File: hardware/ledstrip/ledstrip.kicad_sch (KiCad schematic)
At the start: 11 parts, among them J1 Conn_ARM_JTAG_SWD_10, J2 USB_C_Receptacle_USB2.0_16P, U1 STM32G030K6Tx, U2 CP2102N-A02-GQFN20, U3 STUSB4500QTR, U4 USBLC6-2SC6

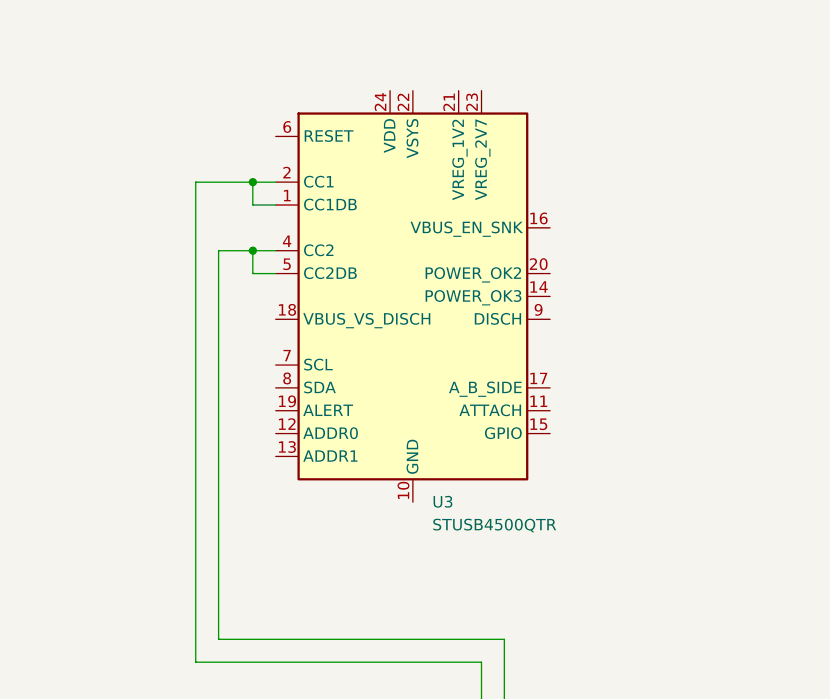
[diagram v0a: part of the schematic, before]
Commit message: Minor improvements, add I2C header for STUSB4500
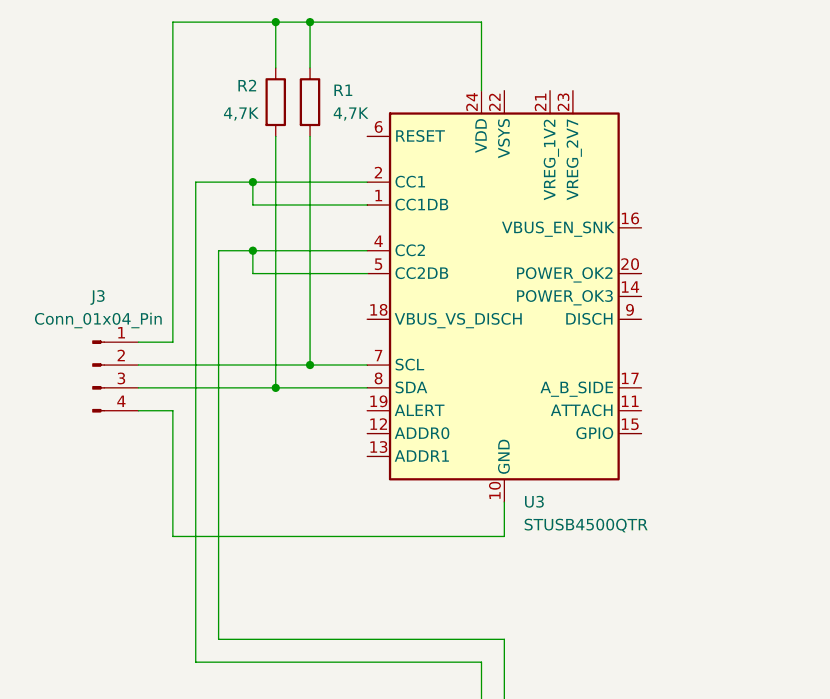
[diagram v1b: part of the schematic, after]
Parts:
- added J3: Conn_01x04_Pin, Connector_PinHeader_2.54mm:PinHeader_1x04_P2.54mm_Vertical, symbol Connector:Conn_01x04_Pin
- added R1, R2: 4,7K, symbol Device:R
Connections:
- net at U3.10 (GND), U3.25 (GND): now also J3.4 (Pin_4)
- net at U3.24 (VDD): now also J3.1 (Pin_1), R1.1, R2.1
- net at U3.7 (SCL): now also J3.2 (Pin_2), R1.2
- net at U3.8 (SDA): now also J3.3 (Pin_3), R2.2
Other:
- moved on the sheet: U3

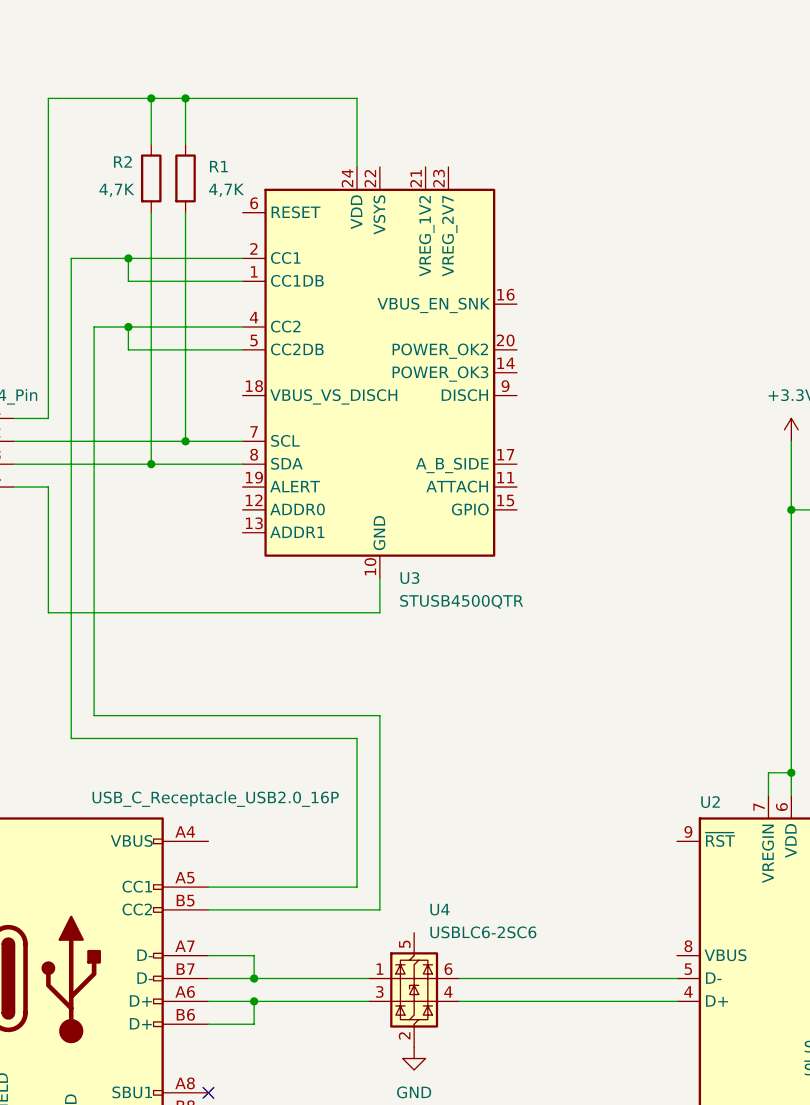
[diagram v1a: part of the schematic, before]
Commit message: Add TVS on CC lines, select a footprint for resistors.
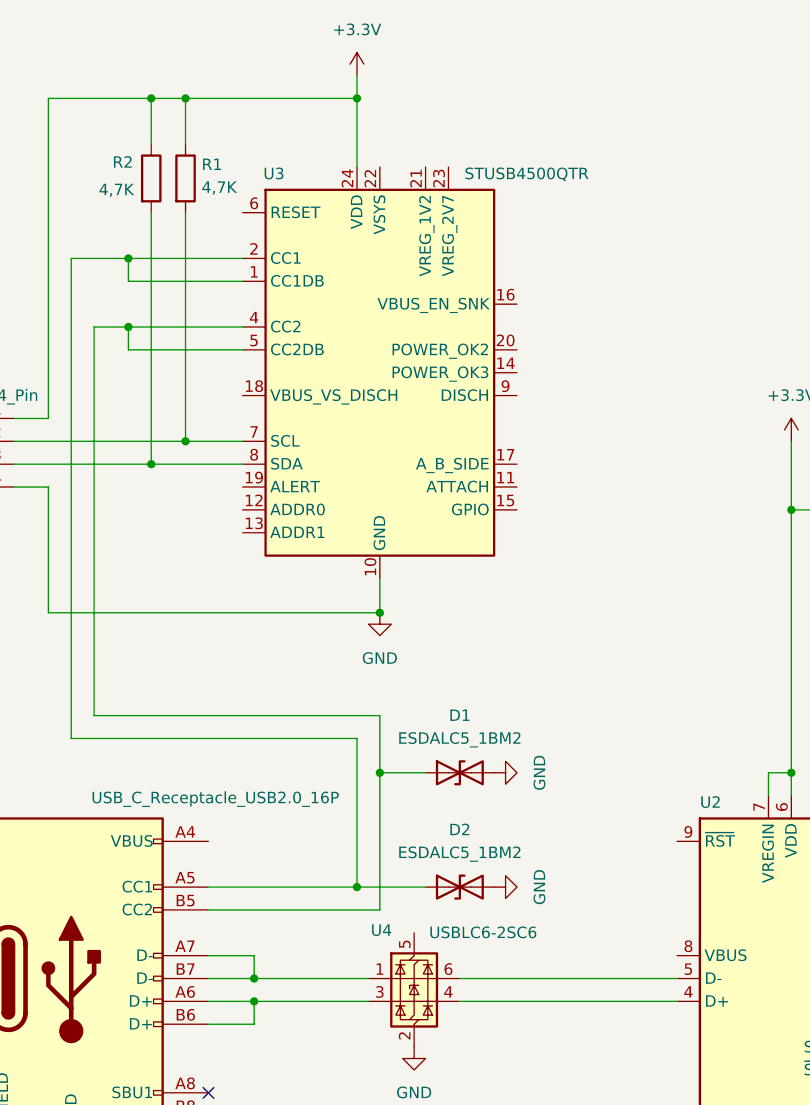
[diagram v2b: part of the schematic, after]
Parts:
- added D1, D2: ESDALC5_1BM2, Diode_SMD:D_SOD-882, symbol Device:D_TVS
- R1, R2: footprint (none) -> Resistor_SMD:R_0805_2012Metric; Distributor Link 1 (none) -> https://www.mouser.fr/ProductDetail/Panasonic/ERA-6ARW472V?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; Distributor Link 2 (none) -> https://www.digikey.com/en/products/detail/panasonic-electr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
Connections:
- net +3.3V: now also J3.1 (Pin_1), R1.1, R2.1, U3.24 (VDD)
- net GND: now also J3.4 (Pin_4), U3.10 (GND), U3.25 (GND), D1.2 (A2), D2.2 (A2)
- net at J2.A5 (CC1), U3.1 (CC1DB), U3.2 (CC1): now also D2.1 (A1)
- net at J2.B5 (CC2), U3.4 (CC2), U3.5 (CC2DB): now also D1.1 (A1)

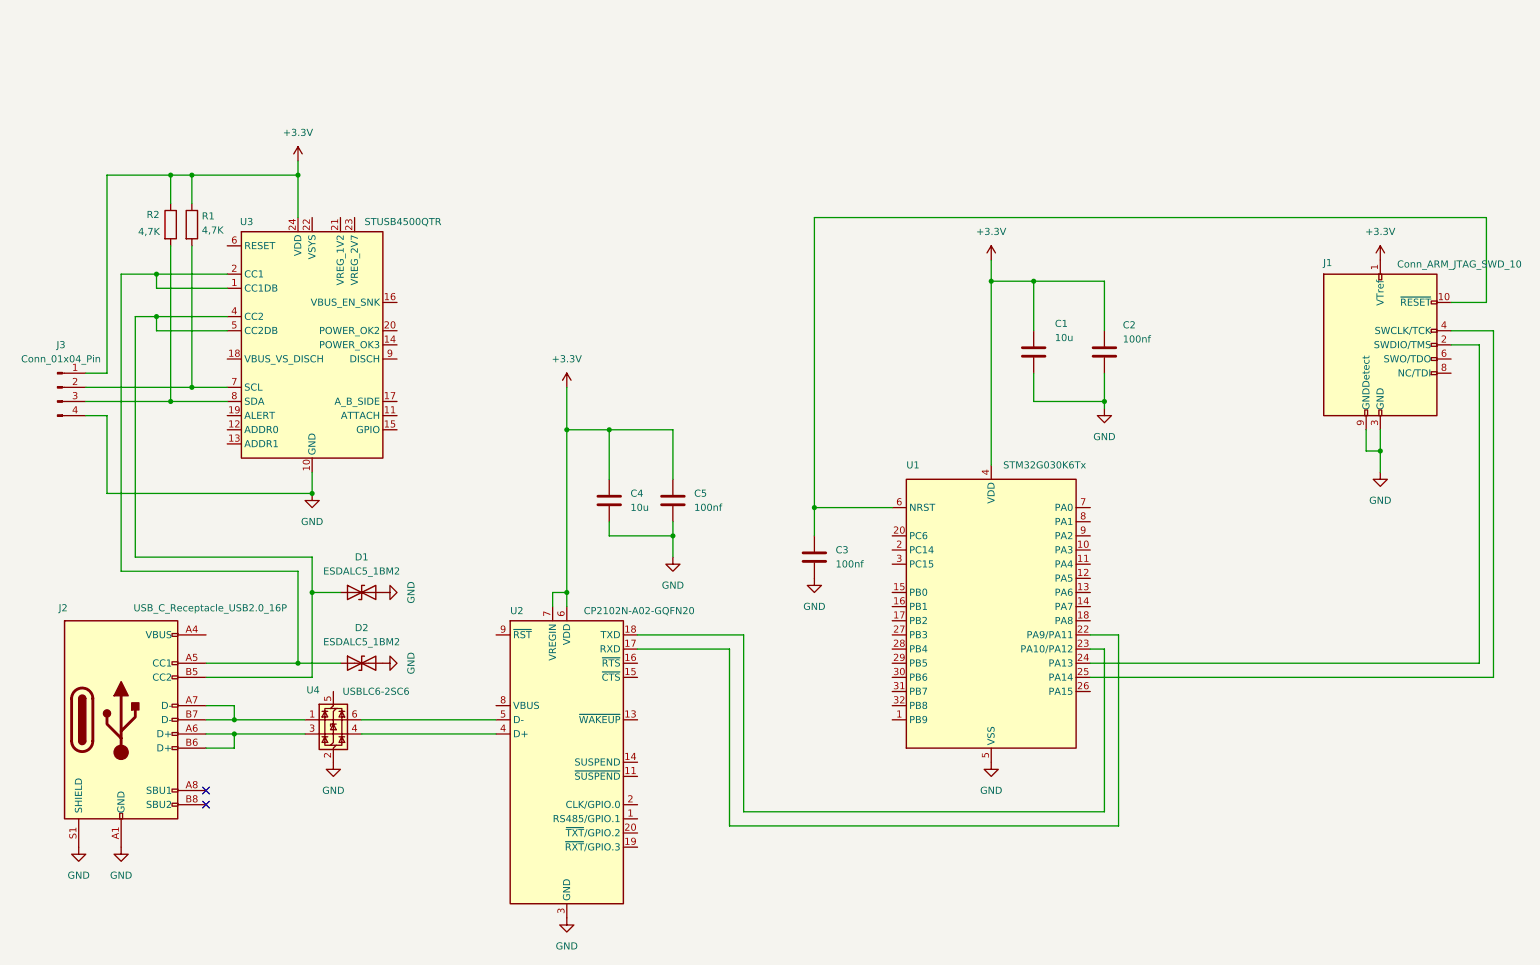
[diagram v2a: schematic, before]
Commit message: Sheet rework, new symbols
Create and add symbol for BQ25703N
Add symbol for BMS interface
Add symbol for LED strip socket
Move power management related things into sub-sheet.
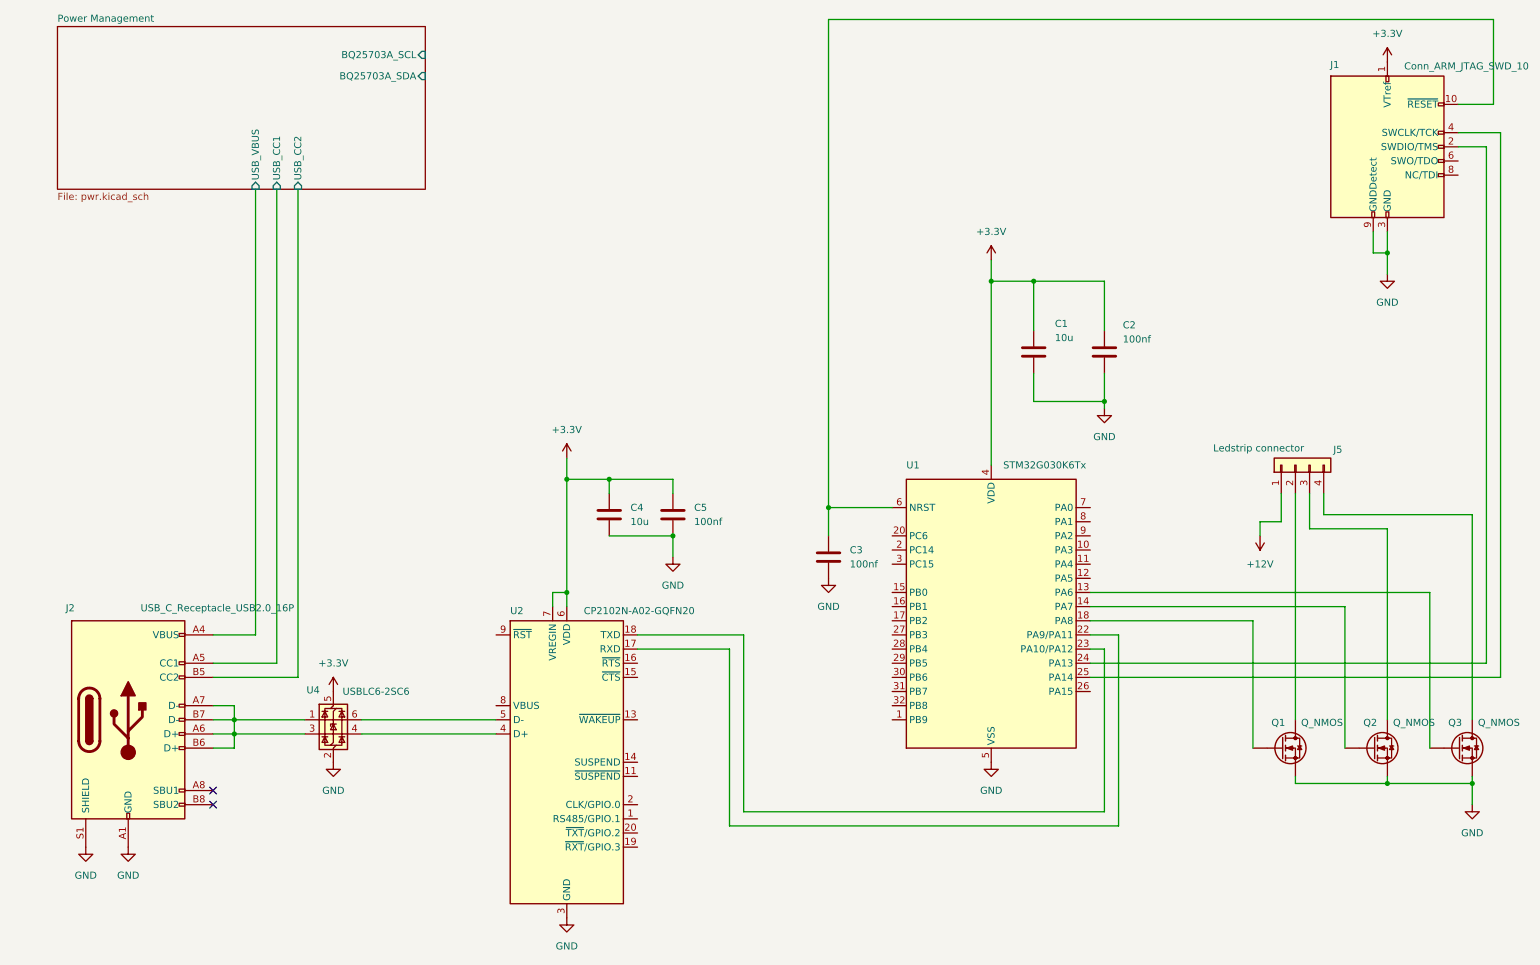
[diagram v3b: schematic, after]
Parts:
- removed D1, D2: ESDALC5_1BM2, Diode_SMD:D_SOD-882, symbol Device:D_TVS
- removed J3: Conn_01x04_Pin, Connector_PinHeader_2.54mm:PinHeader_1x04_P2.54mm_Vertical, symbol Connector:Conn_01x04_Pin
- removed R1, R2: 4,7K, Resistor_SMD:R_0805_2012Metric, symbol Device:R
- removed U3: STUSB4500QTR, Package_DFN_QFN:QFN-24-1EP_4x4mm_P0.5mm_EP2.7x2.7mm, symbol Interface_USB:STUSB4500QTR
- added J5: Ledstrip connector, Connector_JST:JST_XH_B4B-XH-A_1x04_P2.50mm_Vertical, symbol Connector_Generic:Conn_01x04
- added Q1, Q2, Q3: Q_NMOS, Package_TO_SOT_SMD:SOT-23_Handsoldering, symbol Device:Q_NMOS
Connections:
- net +3.3V: now also U4.5 (VBUS)
- net GND: now also Q1.S, Q2.S, Q3.S
- net Power Management/USB_VBUS: now reaches J2.A4 (VBUS), J2.A9 (VBUS), J2.B4 (VBUS), J2.B9 (VBUS)
- net Power Management/USB_CC1: now reaches J2.A5 (CC1)
- net at J2.A6 (D+), J2.B6 (D+), U4.3 (I/O2): now also J2.A7 (D-), J2.B7 (D-), U4.1 (I/O1)
- net Power Management/USB_CC2: now reaches J2.B5 (CC2)
- net at U1.13 (PA6): now also Q3.G
- net at U1.14 (PA7): now also Q2.G
- net at U1.18 (PA8): now also Q1.G
- new net: J5.3 (Pin_3), Q2.D
- new net: J5.2 (Pin_2), Q1.D
- new net: J5.4 (Pin_4), Q3.D
- new net +12V: J5.1 (Pin_1)
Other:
- added sheet Power Management (pwr.kicad_sch)
- moved on the sheet: C3, C4, C5, J1, J2

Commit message: Select part and add potentiometers to schematics.
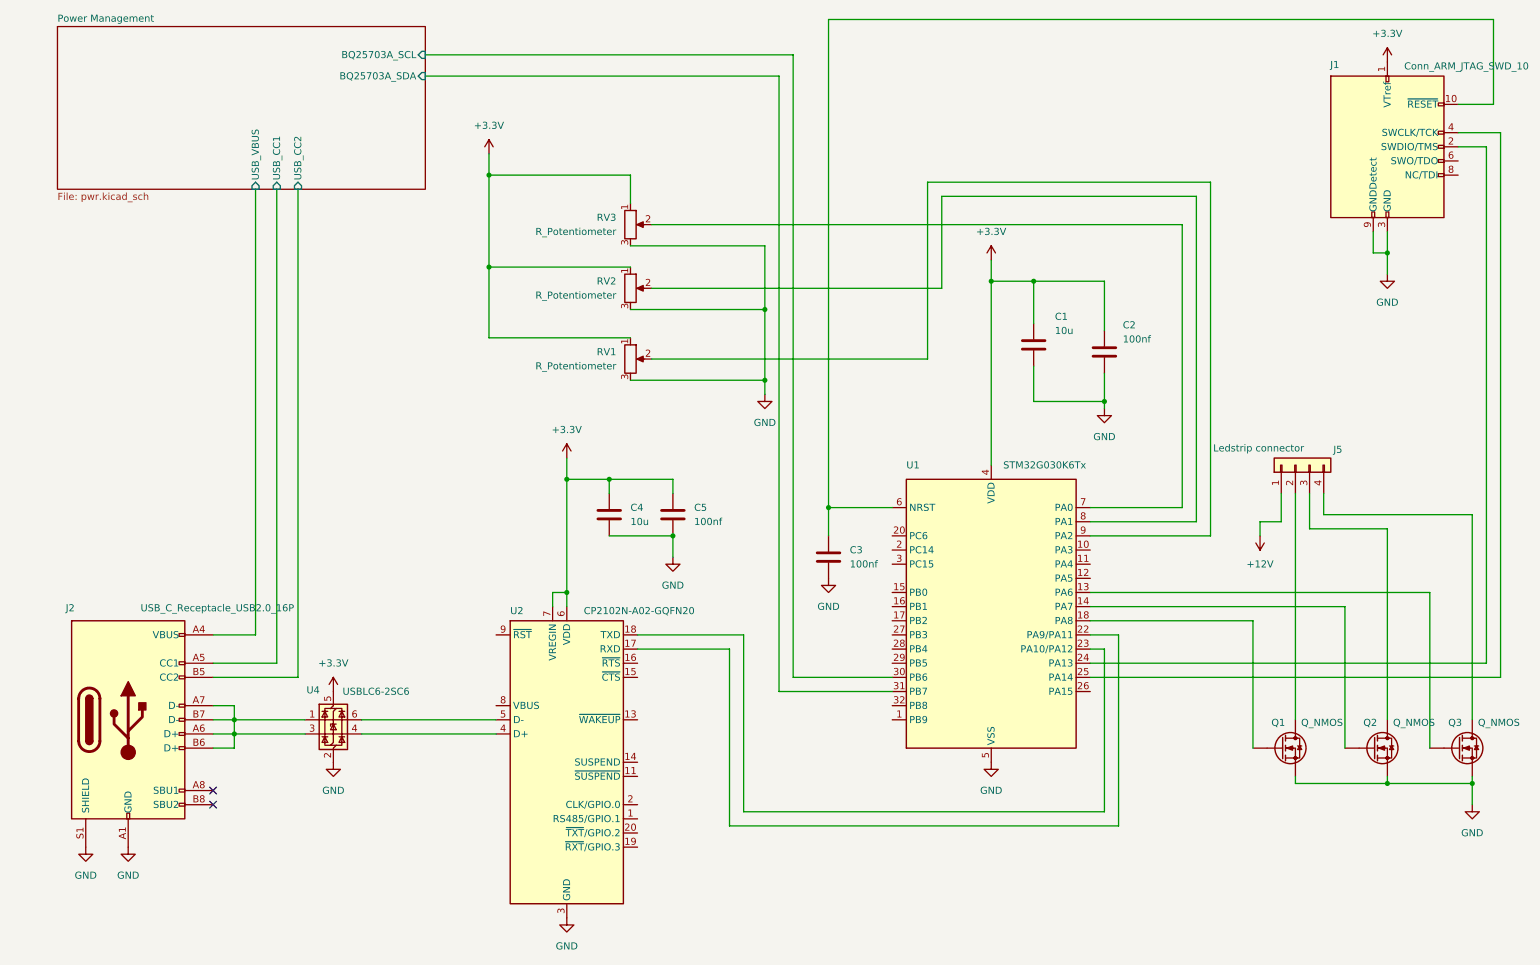
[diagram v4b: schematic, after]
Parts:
- added RV1, RV2, RV3: R_Potentiometer, Potentiometer_THT:Potentiometer_Bourns_PTV09A-1_Single_Vertical, symbol Device:R_Potentiometer
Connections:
- net +3.3V: now also RV1.1, RV2.1, RV3.1
- net GND: now also RV1.3, RV2.3, RV3.3
- net Power Management/BQ25703A_SCL: now also U1.30 (PB6)
- net Power Management/BQ25703A_SDA: now also U1.31 (PB7)
- net at U1.7 (PA0): now also RV3.2
- net at U1.8 (PA1): now also RV2.2
- net at U1.9 (PA2): now also RV1.2
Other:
- moved on the sheet: C1
